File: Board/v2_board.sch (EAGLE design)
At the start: 31 parts, among them T3 BC337, U1 LF33CDT-TR, U2 ESP12, X2 MSTBA11

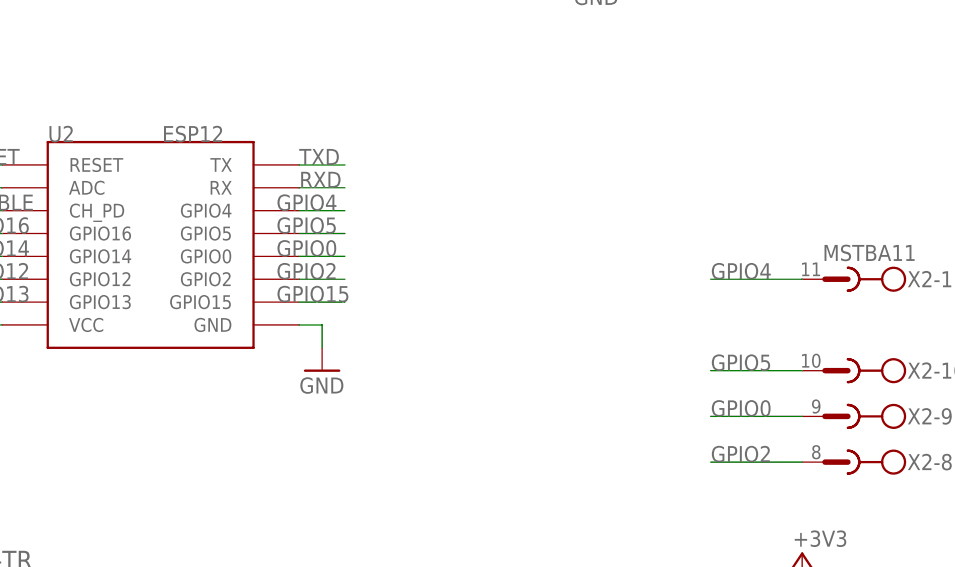
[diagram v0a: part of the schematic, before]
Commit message: fixed library esp12
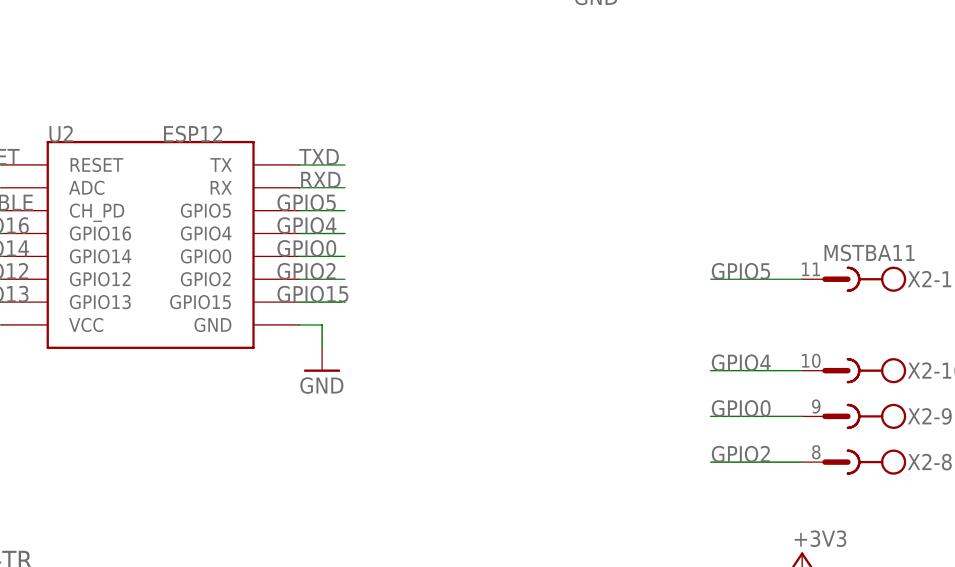
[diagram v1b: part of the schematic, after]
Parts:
- U2: SPICEPREFIX (none) -> X
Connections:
- net GPIO4: now also X2-10.1; no longer X2-11.1
- net GPIO5: now also X2-11.1; no longer X2-10.1
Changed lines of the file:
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@@
 <part name="R14" library="rcl" library_urn="urn:adsk.eagle:library:334" deviceset="R-EU_" device="R1206" package3d_urn="urn:adsk.eagle:package:23540/2" value="1k"/>
 <part name="BUZZER" library="pinhead" library_urn="urn:adsk.eagle:library:325" deviceset="PINHD-1X2" device="" package3d_urn="urn:adsk.eagle:package:22435/2"/>
-<part name="U2" library="esp826612q" deviceset="ESP12" device=""/>
+<part name="U2" library="esp826612q" deviceset="ESP12" device="">
+<attribute name="SPICEPREFIX" value="X"/>
+</part>
 <part name="12V_IN" library="con-phoenix-508" library_urn="urn:adsk.eagle:library:176" deviceset="MSTBA2" device="" package3d_urn="urn:adsk.eagle:package:9615/1"/>
 <part name="+3V8" library="supply1" library_urn="urn:adsk.eagle:library:371" deviceset="+3V3" device=""/>
@@
 <net name="GPIO4" class="0">
 <segment>
-<wire x1="101.6" y1="88.9" x2="106.68" y2="88.9" width="0.1524" layer="91"/>
-<label x="99.06" y="88.9" size="1.778" layer="95"/>
+<wire x1="157.48" y1="71.12" x2="147.32" y2="71.12" width="0.1524" layer="91"/>
+<label x="147.32" y="71.12" size="1.778" layer="95"/>
+<pinref part="X2" gate="-10" pin="1"/>
+</segment>
+<segment>
+<wire x1="101.6" y1="86.36" x2="106.68" y2="86.36" width="0.1524" layer="91"/>
+<label x="99.06" y="86.36" size="1.778" layer="95"/>
 <pinref part="U2" gate="G$1" pin="GPIO4"/>
 </segment>
+</net>
+<net name="GPIO5" class="0">
 <segment>
 <wire x1="157.48" y1="81.28" x2="147.32" y2="81.28" width="0.1524" layer="91"/>
@@
 <pinref part="X2" gate="-11" pin="1"/>
 </segment>
-</net>
-<net name="GPIO5" class="0">
-<segment>
-<wire x1="101.6" y1="86.36" x2="106.68" y2="86.36" width="0.1524" layer="91"/>
-<label x="99.06" y="86.36" size="1.778" layer="95"/>
+<segment>
+<wire x1="101.6" y1="88.9" x2="106.68" y2="88.9" width="0.1524" layer="91"/>
+<label x="99.06" y="88.9" size="1.778" layer="95"/>
 <pinref part="U2" gate="G$1" pin="GPIO5"/>
 </segment>
-<segment>
-<wire x1="157.48" y1="71.12" x2="147.32" y2="71.12" width="0.1524" layer="91"/>
-<label x="147.32" y="71.12" size="1.778" layer="95"/>
-<pinref part="X2" gate="-10" pin="1"/>
-</segment>
-</net>
+</net>

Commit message: Update
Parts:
- renumbered X2 to J1
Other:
- moved on the sheet: 12V_IN-1, 12V_IN-2, AUTO-LED, BUZ-POW, BUZZER, C1, C2, C4, D2, D3, LED-GND, MAN-LED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
